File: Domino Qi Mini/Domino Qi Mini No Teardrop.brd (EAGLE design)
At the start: 55.9 x 33 mm, 94 parts, among them J1 MH22-1, J2 MH22-1, M1 DOMINO, Q1 AP2302GN, Q2 2SC4081, SW1 IT-1210, SW2 IT-1210, SW3 IT-1210, U1 MP65151DJ, U2 ATMEGA32U4-XUAU/MU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

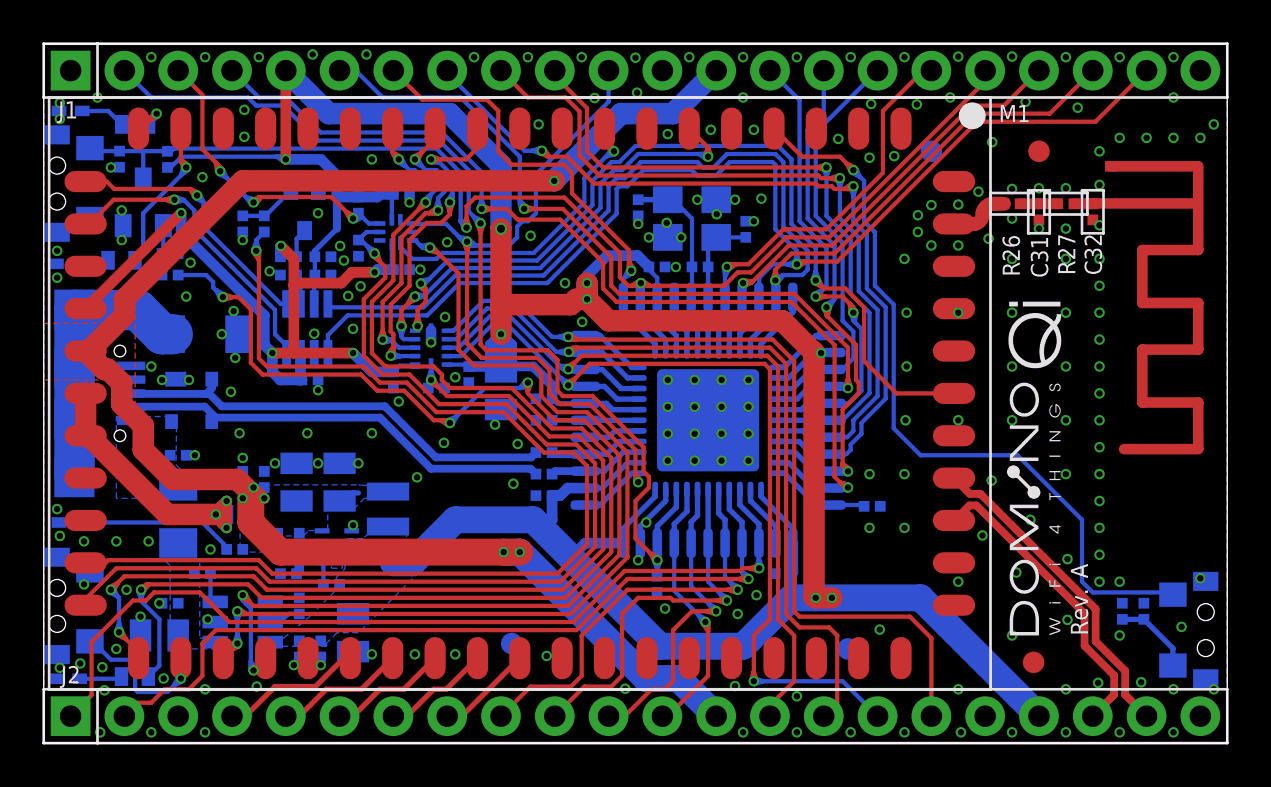
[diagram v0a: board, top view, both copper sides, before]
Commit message: Domino Qi Mini rev. A: eventually no more airwires
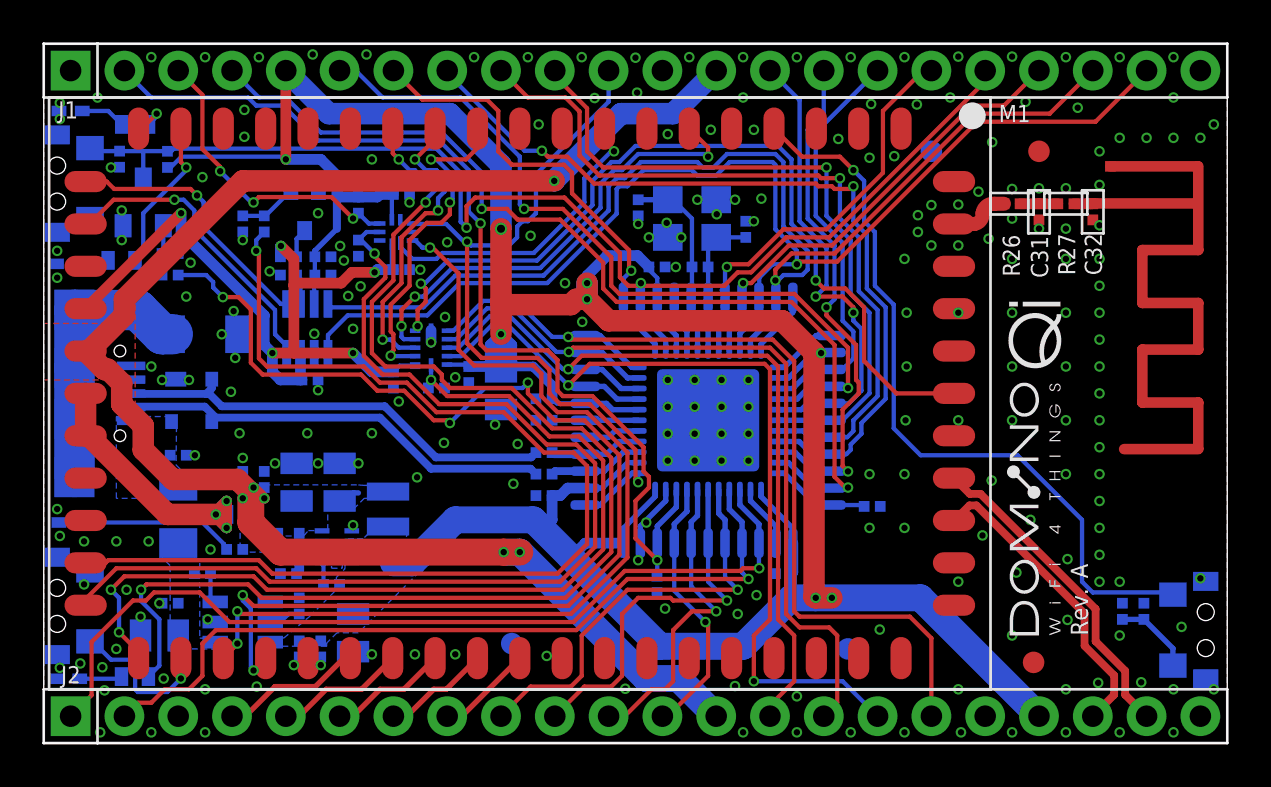
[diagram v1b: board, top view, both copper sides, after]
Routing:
- net I2S_CK: track 67.6 -> 56.1 mm
- net I2S_MCK: track 50.4 -> 43.5 mm
- net LED8: track 22.9 -> 16.0 mm
- net LED7: track 21.3 -> 14.4 mm
- net JTAG_TMS: track 28.8 -> 21.9 mm
- net I2S_WS: track 50.9 -> 44.0 mm
- net LED6: track 66.1 -> 59.2 mm
- net GP6: track 21.4 -> 14.5 mm
- net SS: track 45.8 -> 40.0 mm
- net UART_RTS: track 45.8 -> 40.1 mm
- net AREF: track 50.6 -> 44.9 mm
- net !RESET: track 61.2 -> 55.5 mm
- net IO13: track 48.0 -> 43.4 mm
- net D6: track 24.3 -> 19.8 mm
- net IO12: track 38.9 -> 34.3 mm
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
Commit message: Domino Qi Mini Rev. A: changes in bottom silkscreen
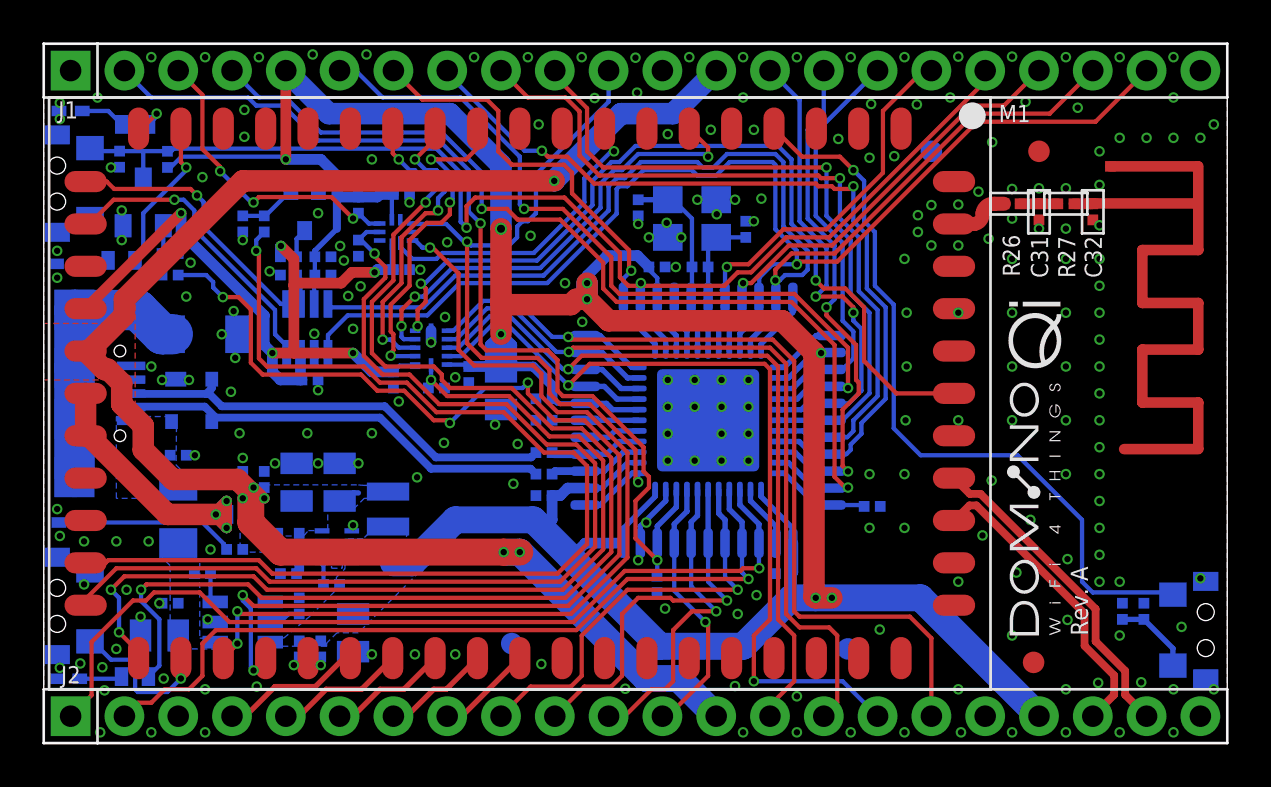
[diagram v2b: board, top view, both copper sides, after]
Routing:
- net GND: track 5.52 -> 4.81 mm, vias 235 -> 234
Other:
- board text removed: "SPI"

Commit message: Domino Qi Mini Rev. A: added BOM and a few datasheets
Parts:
- U2: value ATMEGA32U4-XUAU/MU -> ATMEGA32U4-AU/MU
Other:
- board text removed: "+3V3"
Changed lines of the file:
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@@
 <text x="54.61" y="30.353" size="0.8128" layer="22" rot="MR270" align="center-left">GND</text>
 <text x="34.29" y="30.353" size="0.8128" layer="22" rot="MR270" align="center-left">6~</text>
-<text x="-2.159" y="34.163" size="0.8128" layer="22" rot="MR270" align="center-left">+3V3</text>
 <text x="5.08" y="32.893" size="0.8128" layer="22" rot="MR270" align="center-left">AREF</text>
 <text x="2.667" y="32.893" size="0.8128" layer="22" rot="MR270" align="center-left">GND</text>
@@
 <attribute name="VALUE" x="29.718" y="24.384" size="0.8128" layer="28" rot="MR180"/>
 </element>
-<element name="U2" library="Domino" package="ATMEGA32U4_DUAL_FOOTPRINT" value="ATMEGA32U4-XUAU/MU" x="31.369" y="15.24" smashed="yes" rot="MR180">
+<element name="U2" library="Domino" package="ATMEGA32U4_DUAL_FOOTPRINT" value="ATMEGA32U4-AU/MU" x="31.369" y="15.24" smashed="yes" rot="MR180">
 <attribute name="NAME" x="26.543" y="10.033" size="0.8128" layer="26" rot="MR0" align="center-left"/>
 <attribute name="VALUE" x="25.019" y="22.86" size="0.8128" layer="28" rot="MR180" align="center-left"/>
+<attribute name="PARTNO" value="ATMEGA32U4-MU" x="31.369" y="15.24" size="1.778" layer="28" rot="MR180" display="off"/>
 </element>
 <element name="C15" library="Domino" package="C0402" value="100n" x="28.956" y="22.479" smashed="yes" rot="MR180">
@@
 <attribute name="NAME" x="31.242" y="26.797" size="0.8128" layer="26" rot="MR0"/>
 <attribute name="VALUE" x="27.432" y="23.495" size="0.8128" layer="28" rot="MR90"/>
+<attribute name="PARTNO" value="CRYSTAL_16MHZ_32X25_2SH_12PF_30PPM" x="30.607" y="24.765" size="1.778" layer="28" rot="MR90" display="off"/>
 </element>
 <element name="R2" library="Domino" package="R0402" value="22R" x="23.622" y="12.7" smashed="yes" rot="MR180">
@@
 <attribute name="NAME" x="17.526" y="20.447" size="0.8128" layer="26" rot="MR180" align="center-left"/>
 <attribute name="VALUE" x="17.018" y="20.574" size="0.8128" layer="28" rot="MR180" align="center-left"/>
+<attribute name="PARTNO" value="NTB0104GU12" x="18.288" y="18.669" size="1.778" layer="28" rot="MR180" display="off"/>
 </element>
 <element name="U5" library="Domino" package="XQFN-10" value="NTB0102GU" x="16.637" y="24.13" smashed="yes" rot="MR90">
 <attribute name="NAME" x="18.034" y="24.638" size="0.8128" layer="26" rot="MR180" align="center-left"/>
 <attribute name="VALUE" x="14.732" y="22.225" size="0.8128" layer="28" rot="MR90" align="center-left"/>
+<attribute name="PARTNO" value="NTB0102GU" x="16.637" y="24.13" size="1.778" layer="28" rot="MR90" display="off"/>
 </element>
 <element name="U6" library="Domino" package="SOT23-8" value="MAX3375EEKA+T" x="12.446" y="19.558" smashed="yes" rot="MR0">
 <attribute name="NAME" x="14.097" y="19.431" size="0.8128" layer="26" rot="MR180"/>
 <attribute name="VALUE" x="9.906" y="18.288" size="0.8128" layer="28" rot="MR90"/>
+<attribute name="PARTNO" value="MAX3375EEKA+T" x="12.446" y="19.558" size="1.778" layer="28" rot="MR0" display="off"/>
 </element>
 <element name="C20" library="Domino" package="C0402" value="100n" x="20.066" y="17.399" smashed="yes" rot="MR270">
@@
 <attribute name="NAME" x="11.4865" y="27.486" size="0.8128" layer="26" rot="MR180"/>
 <attribute name="VALUE" x="10.353" y="28.1365" size="0.8128" layer="28" rot="MR180"/>
+<attribute name="PARTNO" value="2SC4081" x="12.319" y="25.146" size="1.778" layer="28" rot="MR180" display="off"/>
 </element>
 <element name="R12" library="Domino" package="R0402" value="10k" x="11.557" y="22.9616" smashed="yes" rot="MR0">
@@
 <attribute name="NAME" x="7.8175" y="25.346" size="0.8128" layer="26" rot="MR0"/>
 <attribute name="VALUE" x="6.665" y="22.5365" size="0.8128" layer="28" rot="MR0"/>
+<attribute name="PARTNO" value="AP2302GN" x="4.699" y="25.527" size="1.778" layer="28" rot="MR0" display="off"/>
 </element>
 <element name="C8" library="Domino" package="C0805" value="2u2" x="21.59" y="16.637" smashed="yes" rot="MR270">
@@
 <attribute name="VOLT" value="6.3V" x="21.59" y="16.637" size="1.778" layer="28" rot="MR270" display="off"/>
 <attribute name="SIZE" value="0402" x="21.59" y="16.637" size="1.778" layer="28" rot="MR270" display="off"/>
-<attribute name="PARTNO" value="C0402_2u2_X5R_20%_CER_6V3" x="21.59" y="16.637" size="1.778" layer="28" rot="MR270" display="off"/>
+<attribute name="PARTNO" value="C0402_2u2_X5R_10%_CER_6V3" x="21.59" y="16.637" size="1.778" layer="28" rot="MR270" display="off"/>
 <attribute name="TYPE" value="CER" x="21.59" y="16.637" size="1.778" layer="28" rot="MR270" display="off"/>
-<attribute name="TOL" value="±20%" x="21.59" y="16.637" size="1.778" layer="28" rot="MR270" display="off"/>
+<attribute name="TOL" value="±10%" x="21.59" y="16.637" size="1.778" layer="28" rot="MR270" display="off"/>
 <attribute name="NAME" x="20.828" y="19.431" size="0.8128" layer="26" rot="MR180"/>
 <attribute name="VALUE" x="24.13" y="18.542" size="0.8128" layer="28" rot="MR270"/>
@@
 <attribute name="NAME" x="0.8128" y="3.2258" size="0.8128" layer="25" ratio="10" align="center-left"/>
 <attribute name="VALUE" x="0" y="-1.27" size="0.8128" layer="27" align="center-left"/>
+<attribute name="PARTNO" value="MH22-1-0.1" x="1.27" y="1.27" size="1.778" layer="27" display="off"/>
 </element>
 <element name="SW3" library="Domino" package="IT-1210" value="IT-1210" x="54.864" y="5.334" smashed="yes" rot="MR90">
 <attribute name="NAME" x="52.959" y="9.652" size="0.8128" layer="26" rot="MR180" align="center-left"/>
 <attribute name="VALUE" x="51.689" y="2.794" size="0.8128" layer="28" rot="MR90" align="center-left"/>
+<attribute name="PARTNO" value="IT-1210" x="54.864" y="5.334" size="1.778" layer="28" rot="MR90" display="off"/>
 </element>
 <element name="SW2" library="Domino" package="IT-1210" value="IT-1210" x="0.635" y="6.477" smashed="yes" rot="MR270">
 <attribute name="NAME" x="4.445" y="10.795" size="0.8128" layer="26" rot="MR270" align="center-left"/>
 <attribute name="VALUE" x="3.81" y="9.017" size="0.8128" layer="28" rot="MR270" align="center-left"/>
+<attribute name="PARTNO" value="IT-1210" x="0.635" y="6.477" size="1.778" layer="28" rot="MR270" display="off"/>
 </element>
 <element name="SW1" library="Domino" package="IT-1210" value="IT-1210" x="0.635" y="26.416" smashed="yes" rot="MR270">
 <attribute name="NAME" x="2.54" y="25.146" size="0.8128" layer="26" rot="MR90" align="center-left"/>
 <attribute name="VALUE" x="3.81" y="28.956" size="0.8128" layer="28" rot="MR270" align="center-left"/>
+<attribute name="PARTNO" value="IT-1210" x="0.635" y="26.416" size="1.778" layer="28" rot="MR270" display="off"/>
 </element>
 <element name="U$3" library="Domino" package="DOMINO_QI_LOGO_SMALL" value="" x="46.99" y="5.08" rot="R90"/>
@@
 <attribute name="BOM" value="EXCLUDE" x="-34.29" y="-46.99" size="1.778" layer="27" display="off"/>
 </element>
-<element name="A1" library="Domino" package="RF_ANT1" value="RF_ANT1" x="49.8602" y="27.2288" rot="R270"/>
+<element name="A1" library="Domino" package="RF_ANT1" value="RF_ANT1" x="49.8602" y="27.2288" rot="R270">
+<attribute name="BOM" value="EXCLUDE" x="49.8602" y="27.2288" size="1.778" layer="27" rot="R270" display="off"/>
+<attribute name="PARTNO" value="RF_ANT1" x="49.8602" y="27.2288" size="1.778" layer="27" rot="R270" display="off"/>
+</element>
 <element name="J1" library="Domino" package="MH22-1-0.1" value="MH22-1" x="1.27" y="31.75" smashed="yes">
 <attribute name="NAME" x="0.6858" y="29.8958" size="0.8128" layer="25" ratio="10" align="center-left"/>
 <attribute name="VALUE" x="0" y="29.21" size="0.8128" layer="27" align="center-left"/>
+<attribute name="PARTNO" value="MH22-1-0.1" x="1.27" y="31.75" size="1.778" layer="27" display="off"/>
 </element>
 <element name="C2" library="Domino" package="C0402" value="100n" x="5.969" y="6.604" smashed="yes" rot="MR0">
